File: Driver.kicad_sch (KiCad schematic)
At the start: 24 parts, among them Q1 C3M0065100K

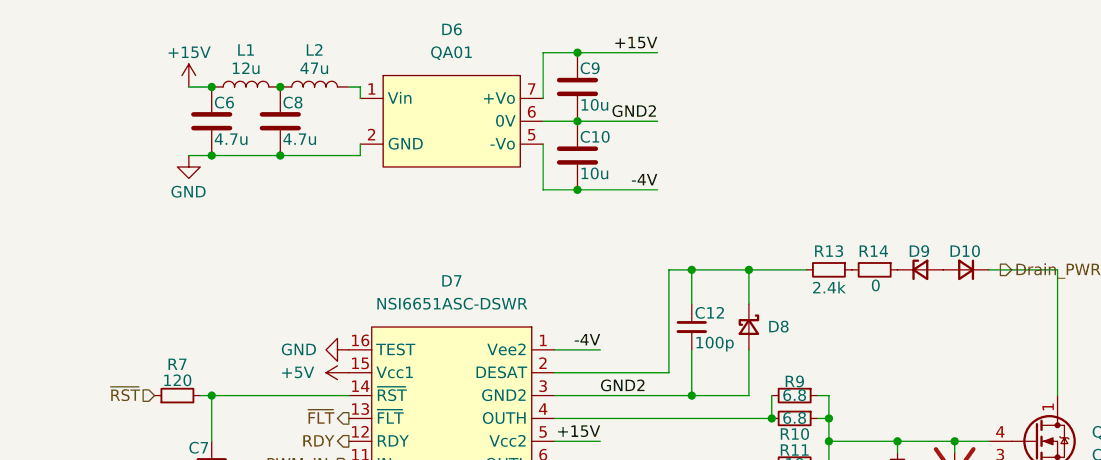
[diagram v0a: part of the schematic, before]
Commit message: VER1.0: убрал источники с платы
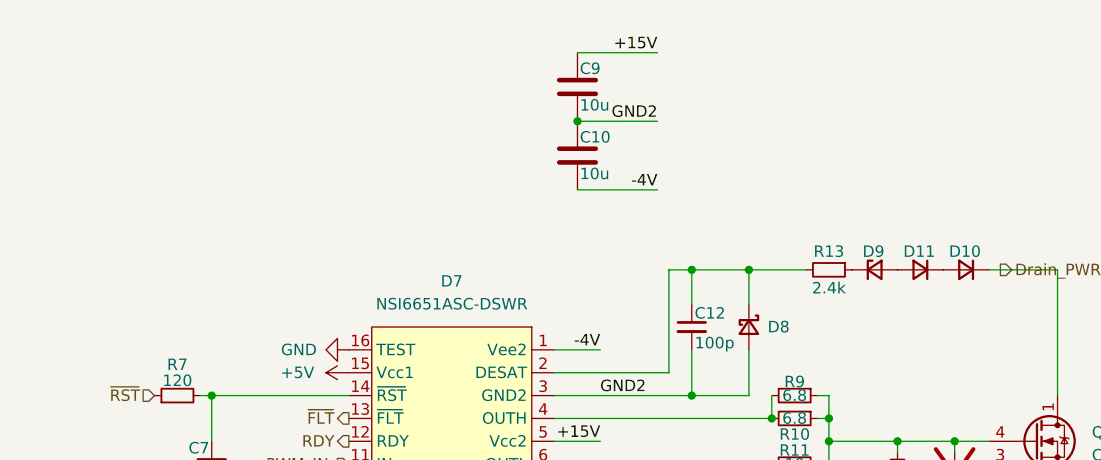
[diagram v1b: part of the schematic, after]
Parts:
- removed C6, C8: 4.7u, Capacitor_SMD:C_1206_3216Metric_Pad1.33x1.80mm_HandSolder, symbol Device:C
- removed D6: QA01, MORNSUN:QA01, symbol MORNSUN:QA
- removed L1: 12u, Inductor_SMD:L_1210_3225Metric_Pad1.42x2.65mm_HandSolder, symbol Device:L
- removed L2: 47u, Inductor_SMD:L_1812_4532Metric_Pad1.30x3.40mm_HandSolder, symbol Device:L
- removed R14: 0, Resistor_SMD:R_0805_2012Metric_Pad1.20x1.40mm_HandSolder, symbol Device:R_Small
- added D11: (no value), Diode_SMD:D_SMA_Handsoldering, symbol Device:D_Small
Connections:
- net at D9.1 (K): now also R13.1
- net at D10.2 (A): now also D11.1 (K); no longer D9.2 (A)
- new net: D11.2 (A), D9.2 (A)
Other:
- moved on the sheet: D9

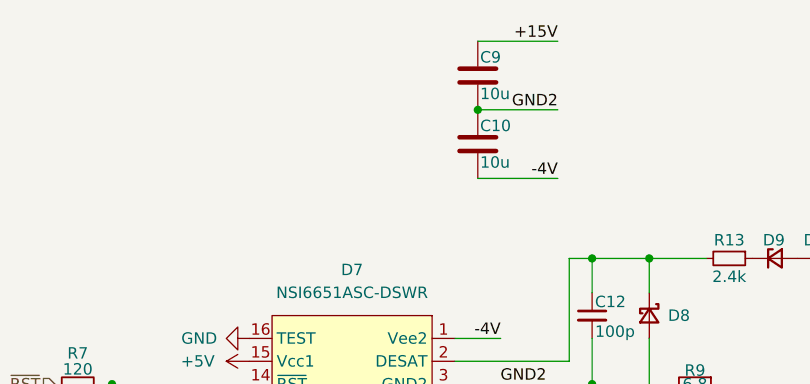
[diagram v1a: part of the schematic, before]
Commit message: VER1.0: добавил разъемы питания
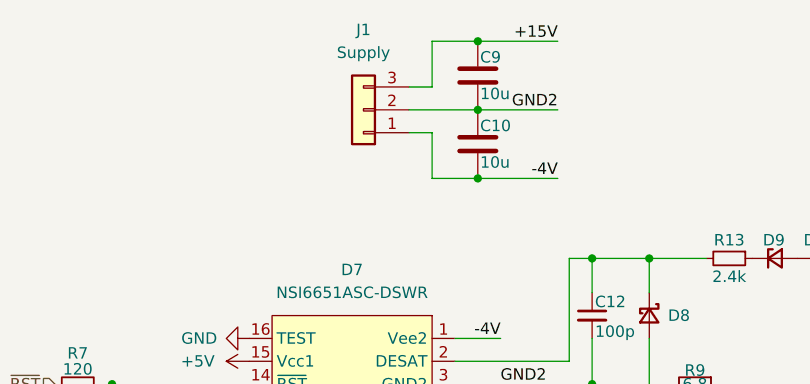
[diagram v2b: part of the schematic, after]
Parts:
- added J1: Supply, Connector_PinSocket_2.54mm:PinSocket_1x03_P2.54mm_Vertical, symbol Connector_Generic:Conn_01x03
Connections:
- net +15V: now also J1.3 (Pin_3)
- net -4V: now also J1.1 (Pin_1)
- net GND2: now also J1.2 (Pin_2)
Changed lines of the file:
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@@
 	(paper "A3")
+	(junction
+		(at 142.24 71.12)
+		(diameter 0)
+		(color 0 0 0 0)
+	)
 	(junction
 		(at 161.29 80.01)
@@
 	)
 	(junction
+		(at 142.24 55.88)
+		(diameter 0)
+		(color 0 0 0 0)
+	)
+	(junction
 		(at 177.8 99.06)
 		(diameter 0)
@@
 	(wire
 		(pts
+			(xy 134.62 60.96) (xy 137.16 60.96)
+		)
+		(stroke
+			(width 0)
+			(type default)
+		)
+	)
+	(wire
+		(pts
 			(xy 170.18 93.98) (xy 170.18 96.52)
 		)
@@
 	(wire
 		(pts
+			(xy 137.16 55.88) (xy 142.24 55.88)
+		)
+		(stroke
+			(width 0)
+			(type default)
+		)
+	)
+	(wire
+		(pts
+			(xy 137.16 66.04) (xy 137.16 71.12)
+		)
+		(stroke
+			(width 0)
+			(type default)
+		)
+	)
+	(wire
+		(pts
 			(xy 177.8 99.06) (xy 177.8 100.33)
 		)
@@
 	(wire
 		(pts
+			(xy 134.62 66.04) (xy 137.16 66.04)
+		)
+		(stroke
+			(width 0)
+			(type default)
+		)
+	)
+	(wire
+		(pts
 			(xy 139.7 99.06) (xy 144.78 99.06)
 		)
@@
 	(wire
 		(pts
+			(xy 137.16 60.96) (xy 137.16 55.88)
+		)
+		(stroke
+			(width 0)
+			(type default)
+		)
+	)
+	(wire
+		(pts
 			(xy 142.24 63.5) (xy 151.13 63.5)
 		)
@@
 	(wire
 		(pts
+			(xy 134.62 63.5) (xy 142.24 63.5)
+		)
+		(stroke
+			(width 0)
+			(type default)
+		)
+	)
+	(wire
+		(pts
 			(xy 101.6 99.06) (xy 101.6 93.98)
 		)
@@
 		(pts
 			(xy 170.18 96.52) (xy 170.18 99.06)
+		)
+		(stroke
+			(width 0)
+			(type default)
+		)
+	)
+	(wire
+		(pts
+			(xy 137.16 71.12) (xy 142.24 71.12)
 		)
 		(stroke
@@
 					(unit 1)
 				)
+			)
+		)
+	)
+	(symbol
+		(lib_id "Connector_Generic:Conn_01x03")
+		(at 129.54 63.5 180)
+		(unit 1)
+		(body_style 1)
+		(exclude_from_sim no)
+		(in_bom yes)
+		(on_board yes)
+		(in_pos_files yes)
+		(dnp no)
+		(fields_autoplaced yes)
+		(property "Reference" "J1"
+			(at 129.54 54.61 0)
+			(show_name no)
+			(do_not_autoplace no)
+			(effects
+				(font
+					(size 1.27 1.27)
+				)
+			)
+		)
+		(property "Value" "Supply"
+			(at 129.54 57.15 0)
+			(show_name no)
+			(do_not_autoplace no)
+			(effects
+				(font
+					(size 1.27 1.27)
+				)
+			)
+		)
+		(property "Footprint" "Connector_PinSocket_2.54mm:PinSocket_1x03_P2.54mm_Vertical"
+			(at 129.54 63.5 0)
+			(hide yes)
+			(show_name no)
+			(do_not_autoplace no)
+			(effects
+				(font
+					(size 1.27 1.27)
+				)
+			)
+		)
+		(property "Datasheet" ""
+			(at 129.54 63.5 0)
+			(hide yes)
+			(show_name no)
+			(do_not_autoplace no)
+			(effects
+				(font
+					(size 1.27 1.27)
+				)
+			)
+		)
+		(property "Description" "Generic connector, single row, 01x03, script generated (kicad-library-utils/schlib/autogen/connector/)"
+			(at 129.54 63.5 0)
+			(hide yes)
+			(show_name no)
+			(do_not_autoplace no)
+			(effects
+				(font
+					(size 1.27 1.27)
+				)
+			)
+		)
+		(pin "2"
+		)
+		(pin "1"
+		)
+		(pin "3"
+		)
+		(instances
+			(project "PSFB_PrimarySide"
+				(path "/52194b95-dcb8-4042-92d9-34956887dcfd/4138c54d-5c98-44b0-b8f1-15d0e26b7a1d"
+					(reference "J1")
+					(unit 1)
+				)
+				(path "/52194b95-dcb8-4042-92d9-34956887dcfd/7b175a7f-50d7-4173-99c1-ddaa7db0110c"
+					(reference "J3")
+					(unit 1)
+				)
+				(path "/52194b95-dcb8-4042-92d9-34956887dcfd/918f2772-cc7c-4283-b6d7-d63090c1e5b4"
+					(reference "J4")
+					(unit 1)
+				)
+				(path "/52194b95-dcb8-4042-92d9-34956887dcfd/973ede4c-8628-4fb0-a639-8e6a770a22fa"
+					(reference "J2")
+					(unit 1)
+				)

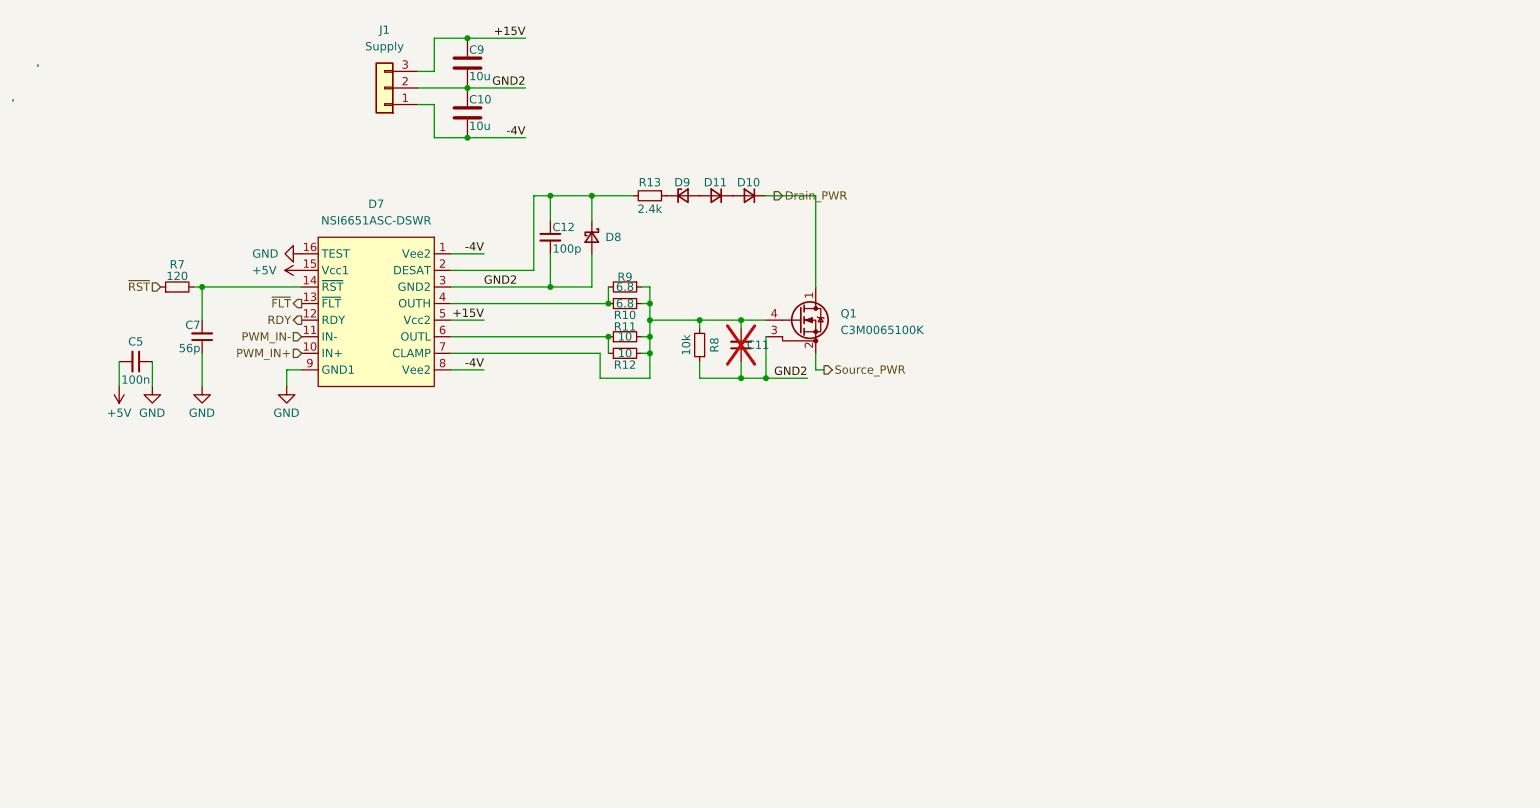
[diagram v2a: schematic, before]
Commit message: VER1.0: развел 4 канала
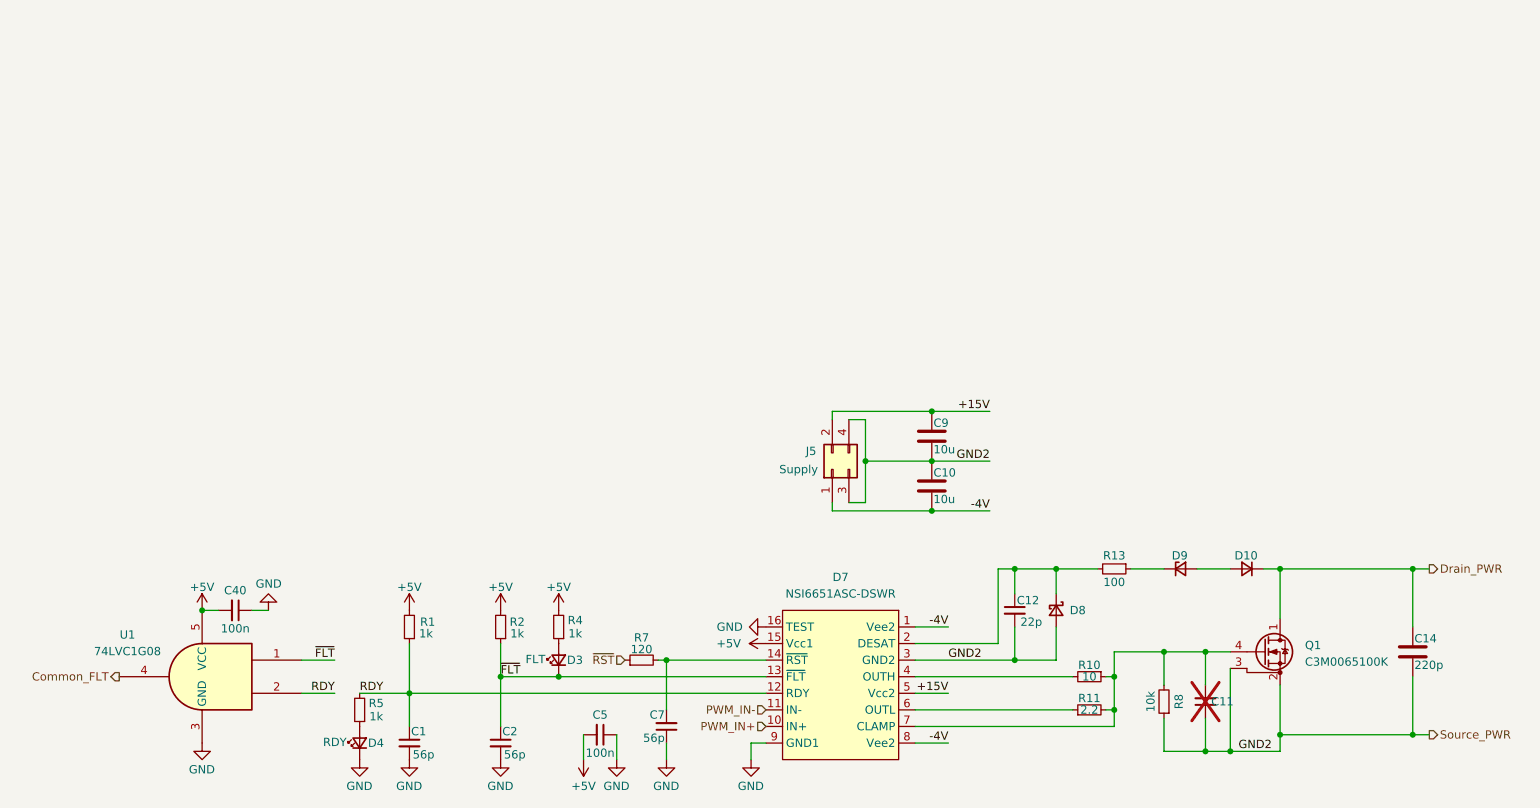
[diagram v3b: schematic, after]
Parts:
- removed D11: (no value), Diode_SMD:D_SMA_Handsoldering, symbol Device:D_Small
- removed J1: Supply, Connector_PinSocket_2.54mm:PinSocket_1x03_P2.54mm_Vertical, symbol Connector_Generic:Conn_01x03
- removed R12: 10, Resistor_SMD:R_1206_3216Metric_Pad1.30x1.75mm_HandSolder, symbol Device:R_Small
- removed R9: 6.8, Resistor_SMD:R_1206_3216Metric_Pad1.30x1.75mm_HandSolder, symbol Device:R_Small
- added C1, C2: 56p, Capacitor_SMD:C_0805_2012Metric_Pad1.18x1.45mm_HandSolder, symbol Device:C_Small
- added C14: 220p, Capacitor_SMD:C_1812_4532Metric_Pad1.57x3.40mm_HandSolder, symbol Device:C
- added C40: 100n, Capacitor_SMD:C_0805_2012Metric_Pad1.18x1.45mm_HandSolder, symbol Device:C_Small
- added D3, D4: (no value), LED_SMD:LED_0805_2012Metric_Pad1.15x1.40mm_HandSolder, symbol Device:LED_Small
- added J5: Supply, Connector_PinSocket_2.54mm:PinSocket_2x02_P2.54mm_Vertical, symbol Connector_Generic:Conn_02x02_Odd_Even
- added R1, R2, R4, R5: 1k, Resistor_SMD:R_0805_2012Metric_Pad1.20x1.40mm_HandSolder, symbol Device:R_Small
- added U1: 74LVC1G08, Package_TO_SOT_SMD:SOT-353_SC-70-5, symbol 74xGxx:74LVC1G08
- C12: value 100p -> 22p
- D10: Product Name MURS160 -> US1M
- D9: footprint Diode_SMD:D_SOD-123 -> Diode_SMD:D_SOD-323_HandSoldering; Product Name MMSZ5232B -> BZT52C2V4S
- R10: value 6.8 -> 10
- R11: value 10 -> 2.2
- R13: value 2.4k -> 100
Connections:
- net GND2 is gone; now on net Source_PWR: C10.1, C11.1, C12.2, C9.2, D7.3 (GND2), D8.2 (A), Q1.3 (DS), R8.1
- net +15V: now also J5.2 (Pin_2)
- net +5V: now also C40.2, R1.2, R2.2, R4.2, U1.5 (VCC)
- net -4V: now also J5.1 (Pin_1)
- net Drain_PWR: now also C14.1
- net GND: now also C1.2, C2.2, C40.1, D4.1 (K), U1.3 (GND)
- net RDY: now also C1.1, R1.1, R5.2, U1.2
- net Source_PWR: now also C14.2, J5.3 (Pin_3), J5.4 (Pin_4)
- net ~{FLT}: now also C2.1, D3.1 (K), R2.1, U1.1
- net at D10.2 (A): now also D9.2 (A)
- new net: D4.2 (A), R5.1
- new net: D3.2 (A), R4.1
- new net Common_FLT: U1.4
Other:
- moved on the sheet: C10, C11, C12, C5, C7, C9, D10, D7, D8, D9, Q1, R10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

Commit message: VER1.0: добавил разъем под FFC
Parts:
- removed C14: 220p, Capacitor_SMD:C_1812_4532Metric_Pad1.57x3.40mm_HandSolder, symbol Device:C
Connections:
- net +5V renamed +3.3V

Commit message: VER1.0: добавил ресет общий
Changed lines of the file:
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@@
 		(property "Purpose" "RDY"
 			(at 121.92 163.703 90)
+			(hide yes)
 			(show_name no)
 			(do_not_autoplace no)
@@
 		(property "Purpose" "FLT"
 			(at 152.654 151.003 90)
-			(show_name no)
-			(do_not_autoplace no)
+			(hide yes)
+			(show_name no)
+			(do_not_autoplace no)

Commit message: VER1.0: сделал файлы для производства
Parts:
- C1, C11, C12, C2, C40, C5, C7: Description P/N Capacitor SMD 25+V -> Capacitor SMD 50V
- C10, C9: Description P/N Capacitor SMD 50+V -> Capacitor SMD 50V
- D3: Description P/N Red LED -> LEDs
- D4: Description P/N Blue LED -> LEDs
- D7: value NSI6651ASC-DSWR -> (none); Description P/N (none) -> Gate Driver; Product Name (none) -> NSI6651ASC-DSWR
- J5: value Supply -> (none); Description P/N (none) -> Connector; Product Name (none) -> KLS1-208-2-04-S
- Q1: value C3M0065100K -> (none); Description P/N (none) -> SiC Mosfet; Product Name (none) -> C3M0065100K
- U1: value 74LVC1G08 -> (none); Description P/N (none) -> AND; Product Name (none) -> 74LVC1G08
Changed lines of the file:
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@@
 			)
 		)
-		(property "Value" "74LVC1G08"
+		(property "Value" ""
 			(at 90.17 149.7898 0)
 			(show_name no)
@@
 			)
 		)
+		(property "Product Name" "74LVC1G08"
+			(at 101.6 153.67 0)
+			(hide yes)
+			(show_name no)
+			(do_not_autoplace no)
+			(effects
+				(font
+					(size 1.27 1.27)
+				)
+			)
+		)
+		(property "Description P/N" "AND"
+			(at 101.6 153.67 0)
+			(hide yes)
+			(show_name no)
+			(do_not_autoplace no)
+			(effects
+				(font
+					(size 1.27 1.27)
+				)
+			)
+		)
+		(property "Replacement" ""
+			(at 101.6 153.67 0)
+			(hide yes)
+			(show_name no)
+			(do_not_autoplace no)
+			(effects
+				(font
+					(size 1.27 1.27)
+				)
+			)
+		)
+		(property "Function" ""
+			(at 101.6 153.67 0)
+			(hide yes)
+			(show_name no)
+			(do_not_autoplace no)
+			(effects
+				(font
+					(size 1.27 1.27)
+				)
+			)
+		)
 		(pin "2"
 		)
@@
 			)
 		)
-		(property "Description P/N" "Capacitor SMD 25+V"
+		(property "Description P/N" "Capacitor SMD 50V"
 			(at 255.27 157.48 0)
 			(hide yes)
@@
 			)
 		)
-		(property "Value" "NSI6651ASC-DSWR"
+		(property "Value" ""
 			(at 199.39 140.97 0)
 			(show_name no)
@@
 			)
 		)
+		(property "Product Name" "NSI6651ASC-DSWR"
+			(at 199.39 143.51 0)
+			(hide yes)
+			(show_name no)
+			(do_not_autoplace no)
+			(effects
+				(font
+					(size 1.27 1.27)
+				)
+			)
+		)
+		(property "Description P/N" "Gate Driver"
+			(at 199.39 143.51 0)
+			(hide yes)
+			(show_name no)
+			(do_not_autoplace no)
+			(effects
+				(font
+					(size 1.27 1.27)
+				)
+			)
+		)
+		(property "Replacement" ""
+			(at 199.39 143.51 0)
+			(hide yes)
+			(show_name no)
+			(do_not_autoplace no)
+			(effects
+				(font
+					(size 1.27 1.27)
+				)
+			)
+		)
+		(property "Function" ""
+			(at 199.39 143.51 0)
+			(hide yes)
+			(show_name no)
+			(do_not_autoplace no)
+			(effects
+				(font
+					(size 1.27 1.27)
+				)
+			)
+		)
 		(pin "6"
 		)
@@
 			)
 		)
-		(property "Description P/N" "Blue LED"
+		(property "Description P/N" "LEDs"
 			(at 125.73 163.83 0)
 			(hide yes)
@@
 			)
 		)
+		(property "Function" ""
+			(at 125.73 163.83 0)
+			(hide yes)
+			(show_name no)
+			(do_not_autoplace no)
+			(effects
+				(font
+					(size 1.27 1.27)
+				)
+			)
+		)
 		(pin "1"
 		)
@@
 			)
 		)
-		(property "Description P/N" "Capacitor SMD 25+V"
+		(property "Description P/N" "Capacitor SMD 50V"
 			(at 147.32 163.83 0)
 			(hide yes)
@@
 			)
 		)
-		(property "Description P/N" "Red LED"
+		(property "Description P/N" "LEDs"
 			(at 156.21 151.13 0)
 			(hide yes)
@@
 			)
 		)
+		(property "Function" ""
+			(at 156.21 151.13 0)
+			(hide yes)
+			(show_name no)
+			(do_not_autoplace no)
+			(effects
+				(font
+					(size 1.27 1.27)
+				)
+			)
+		)
 		(pin "1"
 		)
@@
 			)
 		)
-		(property "Value" "Supply"
+		(property "Value" ""
 			(at 189.992 121.92 90)
 			(show_name no)
@@
 			)
 		)
+		(property "Product Name" "KLS1-208-2-04-S"
+			(at 198.12 121.92 0)
+			(hide yes)
+			(show_name no)
+			(do_not_autoplace no)
+			(effects
+				(font
+					(size 1.27 1.27)
+				)
+			)
+		)
+		(property "Description P/N" "Connector"
+			(at 198.12 121.92 0)
+			(hide yes)
+			(show_name no)
+			(do_not_autoplace no)
+			(effects
+				(font
+					(size 1.27 1.27)
+				)
+			)
+		)
+		(property "Replacement" ""
+			(at 198.12 121.92 0)
+			(hide yes)
+			(show_name no)
+			(do_not_autoplace no)
+			(effects
+				(font
+					(size 1.27 1.27)
+				)
+			)
+		)
+		(property "Function" ""
+			(at 198.12 121.92 0)
+			(hide yes)
+			(show_name no)
+			(do_not_autoplace no)
+			(effects
+				(font
+					(size 1.27 1.27)
+				)
+			)
+		)
 		(pin "2"
 		)
@@
 			)
 		)
+		(property "Function" ""
+			(at 232.41 143.51 0)
+			(hide yes)
+			(show_name no)
+			(do_not_autoplace no)
+			(effects
+				(font
+					(size 1.27 1.27)
+				)
+			)
+		)
 		(pin "1"
 		)
@@
 			)
 		)
-		(property "Value" "C3M0065100K"
+		(property "Value" ""
 			(at 270.51 151.3966 0)
 			(show_name no)
@@
 			)
 		)
+		(property "Product Name" "C3M0065100K"
+			(at 264.16 149.86 0)
+			(hide yes)
+			(show_name no)
+			(do_not_autoplace no)
+			(effects
+				(font
+					(size 1.27 1.27)
+				)
+			)
+		)
+		(property "Description P/N" "SiC Mosfet"
+			(at 264.16 149.86 0)
+			(hide yes)
+			(show_name no)
+			(do_not_autoplace no)
+			(effects
+				(font
+					(size 1.27 1.27)
+				)
+			)
+		)
+		(property "Replacement" ""
+			(at 264.16 149.86 0)
+			(hide yes)
+			(show_name no)
+			(do_not_autoplace no)
+			(effects
+				(font
+					(size 1.27 1.27)
+				)
+			)
+		)
+		(property "Function" ""
+			(at 264.16 149.86 0)
+			(hide yes)
+			(show_name no)
+			(do_not_autoplace no)
+			(effects
+				(font
+					(size 1.27 1.27)
+				)
+			)
+		)
 		(pin "3"
 		)
@@
 			)
 		)
-		(property "Description P/N" "Capacitor SMD 25+V"
+		(property "Description P/N" "Capacitor SMD 50V"
 			(at 172.72 161.29 0)
 			(hide yes)
@@
 			)
 		)
-		(property "Description P/N" "Capacitor SMD 50+V"
+		(property "Description P/N" "Capacitor SMD 50V"
 			(at 213.36 124.46 0)
 			(hide yes)
@@
 			)
 		)
-		(property "Description P/N" "Capacitor SMD 25+V"
+		(property "Description P/N" "Capacitor SMD 50V"
 			(at 133.35 163.83 0)
 			(hide yes)
@@
 			)
 		)
-		(property "Description P/N" "Capacitor SMD 50+V"
+		(property "Description P/N" "Capacitor SMD 50V"
 			(at 213.36 116.84 0)
 			(hide yes)
@@
 			)
 		)
-		(property "Description P/N" "Capacitor SMD 25+V"
+		(property "Description P/N" "Capacitor SMD 50V"
 			(at 162.56 162.56 0)
 			(hide yes)
@@
 			)
 		)
-		(property "Description P/N" "Capacitor SMD 25+V"
+		(property "Description P/N" "Capacitor SMD 50V"
 			(at 106.68 143.51 0)
 			(hide yes)
@@
 			)
 		)
-		(property "Description P/N" "Capacitor SMD 25+V"
+		(property "Description P/N" "Capacitor SMD 50V"
 			(at 226.06 143.51 0)
 			(hide yes)
